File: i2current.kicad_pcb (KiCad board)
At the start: 2 copper layers, 59 parts, among them J1 Barrel_Jack_Switch, J2 USB_C_Receptacle_USB2.0, J3 CONN_BATT, J4 Lichtenprog_conn, Q1 WST03P06, Q2 MMBT2222A, Q3 MMBT2222A, SW1 SW_SPDT, U1 TPS61022, U2 BQ25606RGER, U3 SPX3819M5-L-3-3, U5 FUSB302B01MPX, U6 XT30(2+2)PW-M.G.B, U7 ESP32-C3-WROOM-02, U8 BQ25792RQMR

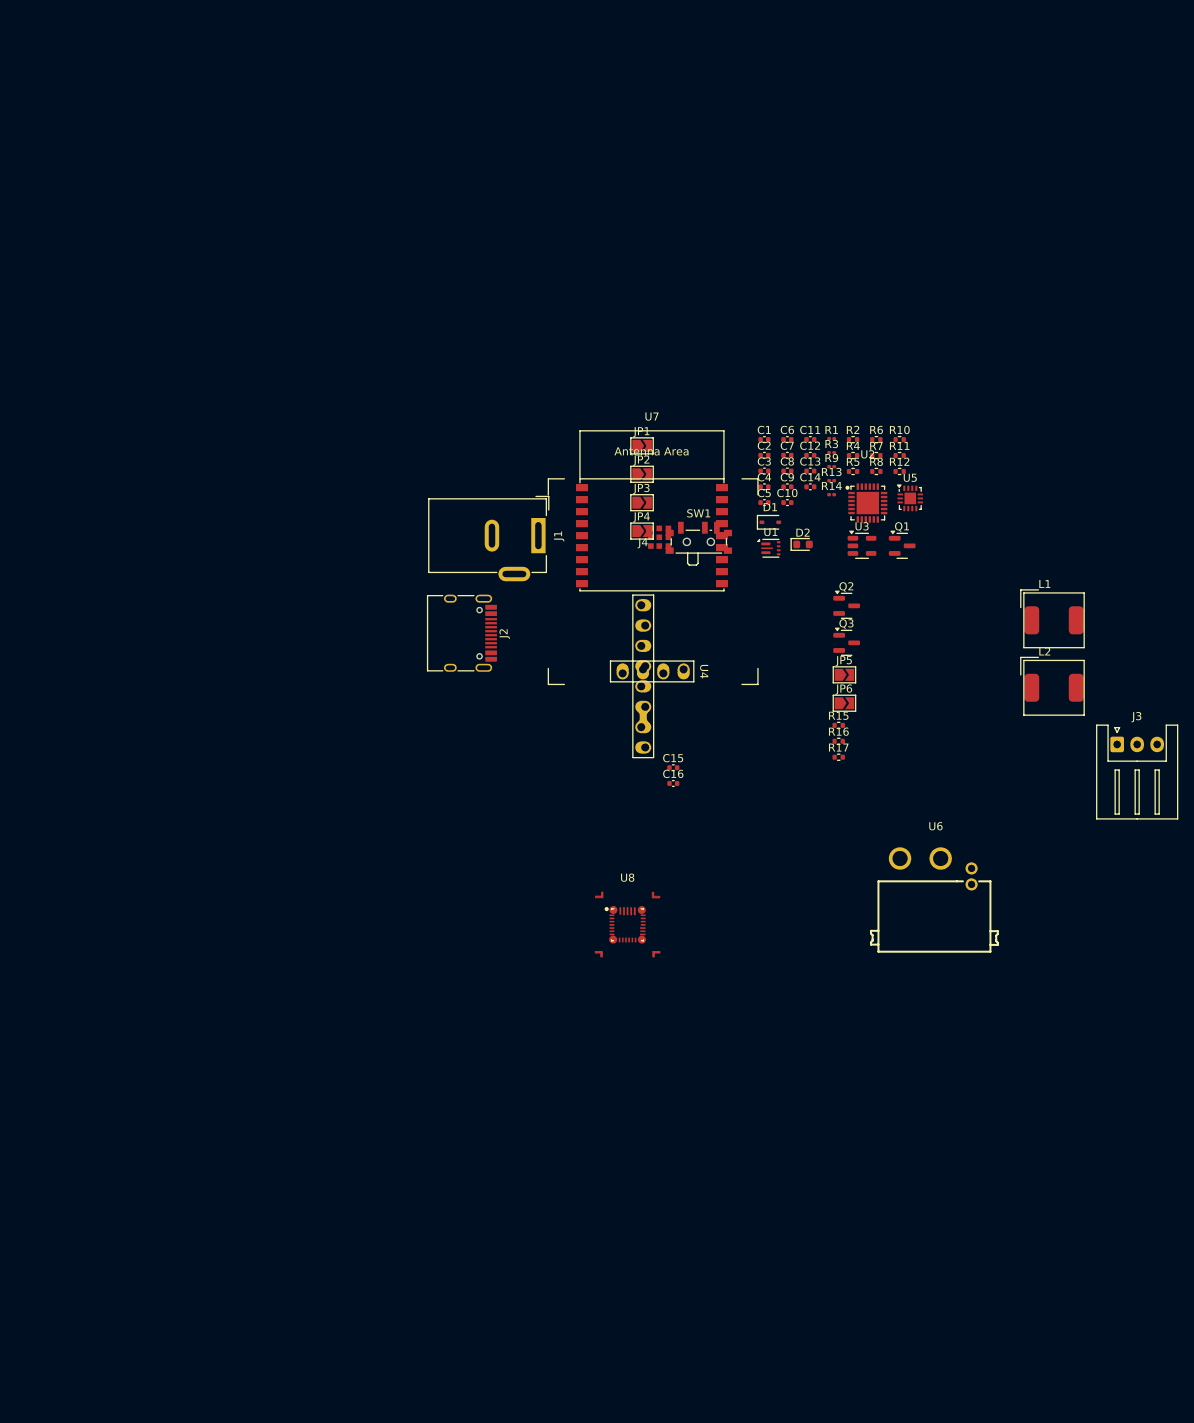
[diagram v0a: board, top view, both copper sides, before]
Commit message: connector placement
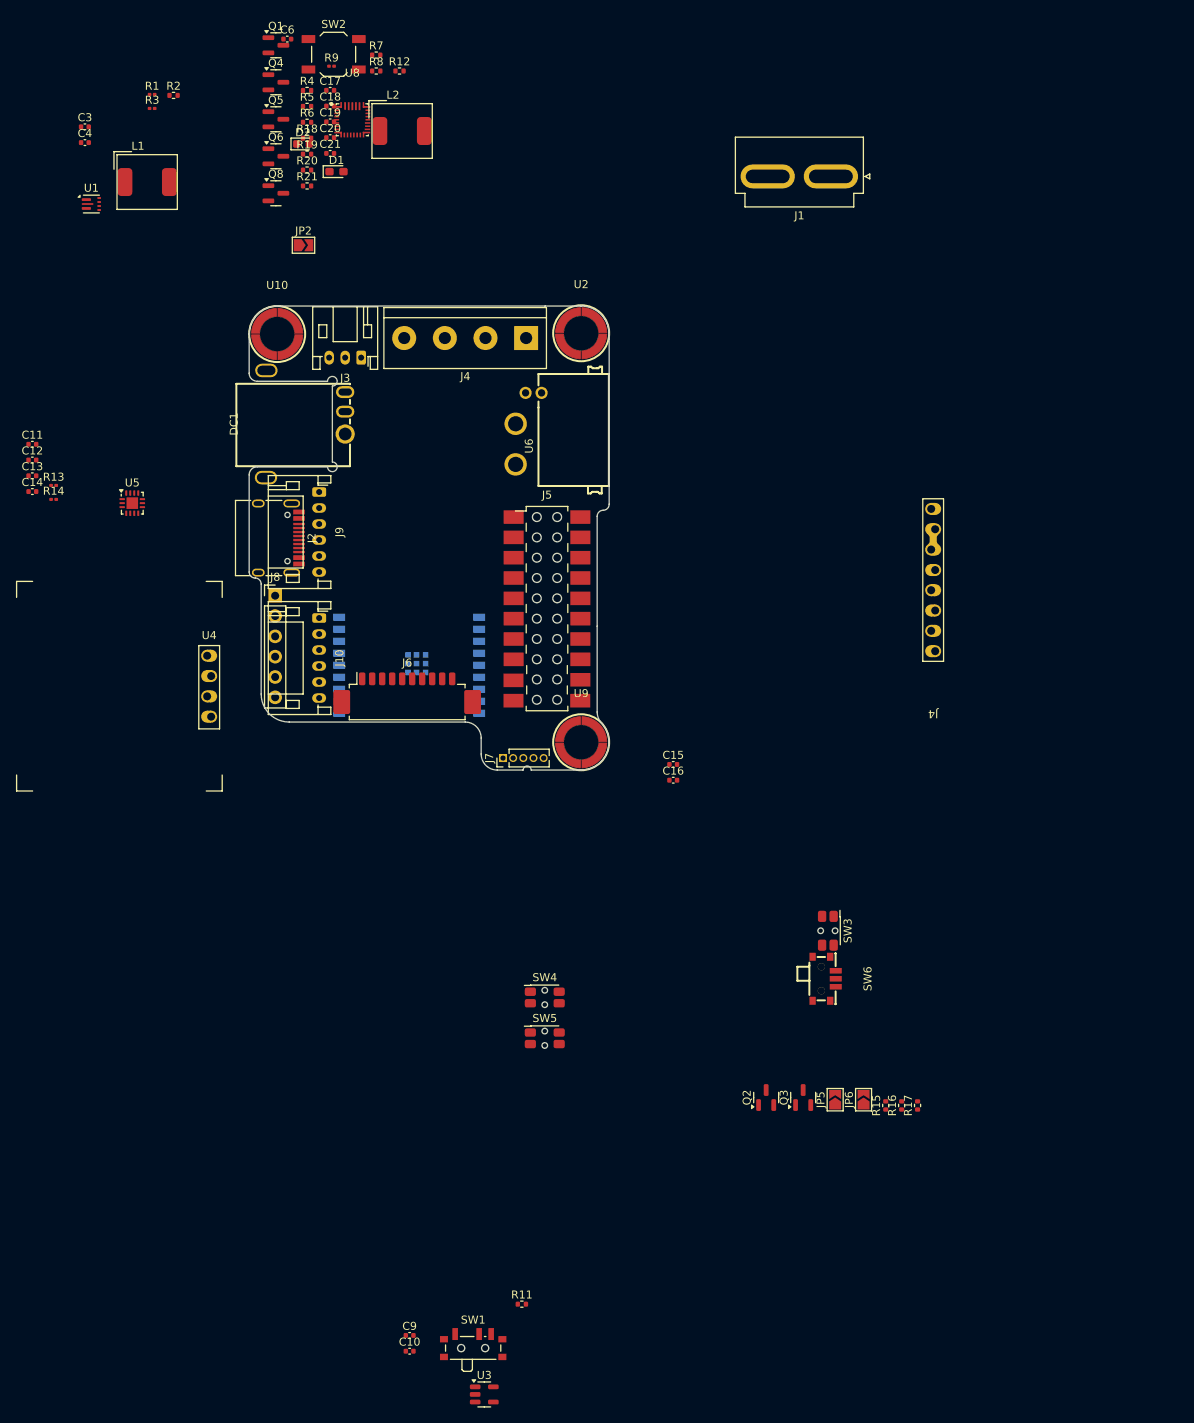
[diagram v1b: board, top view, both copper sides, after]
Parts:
- removed C1: 1u, Capacitor_SMD:C_0402_1005Metric
- removed C2, C8: 10u, Capacitor_SMD:C_0402_1005Metric
- removed C5: 100n, Capacitor_SMD:C_0402_1005Metric
- removed C7: 4.7u, Capacitor_SMD:C_0402_1005Metric
- removed JP1, JP3: SCH_BYP, Jumper:SolderJumper-2_P1.3mm_Open_TrianglePad1.0x1.5mm
- removed JP4: FUSB_INT, Jumper:SolderJumper-2_P1.3mm_Open_TrianglePad1.0x1.5mm
- removed R10: 240, Resistor_SMD:R_0402_1005Metric
- added C17: 10u, Capacitor_SMD:C_0402_1005Metric, F.Cu at (58.1, 27.5)
- added C18: 10u, Capacitor_SMD:C_0402_1005Metric, F.Cu at (58.1, 29.5)
- added C19: 100n, Capacitor_SMD:C_0402_1005Metric, F.Cu at (58.1, 31.5)
- added C20: 100n, Capacitor_SMD:C_0402_1005Metric, F.Cu at (58.1, 33.5)
- added C21: 10u, Capacitor_SMD:C_0402_1005Metric, F.Cu at (58.1, 35.4)
- added DC1: DC-C033D-5.5A-2.0, easyeda2kicad:DC-IN-TH_DC-C033D-5.5A-2.5, F.Cu at (55.1, 69.3)
- added J10: Conn_01x06, Connector_JST:JST_PH_S6B-PH-K_1x06_P2.00mm_Horizontal, F.Cu at (56.8, 93.5)
- added J4: Screw_Terminal_01x04, TerminalBlock:TerminalBlock_bornier-4_P5.08mm, F.Cu at (82.6, 58.5)
- added J5: EXT_IFACE, Critbit_lib:2x10_smdthrough, F.Cu at (85.2, 92.3)
- added J6: Conn_01x10, Connector_Molex:Molex_PicoBlade_53261-1071_1x10-1MP_P1.25mm_Horizontal, F.Cu at (67.8, 103.5)
- added J7: Conn_01x05, Connector_PinHeader_1.27mm:PinHeader_1x05_P1.27mm_Vertical, F.Cu at (79.7, 111.0)
- added J8: Conn_01x06, Connector_PinHeader_2.54mm:PinHeader_1x06_P2.54mm_Vertical, F.Cu at (51.2, 90.7)
- added J9: Conn_01x06, Connector_JST:JST_PH_S6B-PH-K_1x06_P2.00mm_Horizontal, F.Cu at (56.8, 77.8)
- added Q4: AO3400A, Package_TO_SOT_SMD:SOT-23, F.Cu at (51.3, 26.5)
- added Q5: AO3400A, Package_TO_SOT_SMD:SOT-23, F.Cu at (51.3, 31.2)
- added Q6: AO3400A, Package_TO_SOT_SMD:SOT-23, F.Cu at (51.3, 35.8)
- added Q8: AO3400A, Package_TO_SOT_SMD:SOT-23, F.Cu at (51.3, 40.4)
- added R18: 2k, Resistor_SMD:R_0402_1005Metric, F.Cu at (55.2, 33.5)
- added R19: 3k, Resistor_SMD:R_0402_1005Metric, F.Cu at (55.2, 35.5)
- added R20: 3k, Resistor_SMD:R_0402_1005Metric, F.Cu at (55.2, 37.5)
- added R21: 3k, Resistor_SMD:R_0402_1005Metric, F.Cu at (55.2, 39.5)
- added SW2: HARD_RST_BUT, Button_Switch_SMD:SW_SPST_TL3342, F.Cu at (58.6, 23.0)
- added SW3: B2, Button_Switch_SMD:SW_SPST_EVQP7C, F.Cu at (120.3, 132.6)
- added SW4: B2, Button_Switch_SMD:SW_SPST_EVQP7C, F.Cu at (85.0, 140.9)
- added SW5: B2, Button_Switch_SMD:SW_SPST_EVQP7C, F.Cu at (85.0, 146.0)
- added SW6: MINI MSK12CO2, easyeda2kicad:SW-SMD_MSK12CO2, F.Cu at (119.9, 138.6)
- added U10: SMTSO3030CTJ, easyeda2kicad:SMD_BD5.6-D4.1, F.Cu at (51.5, 58.0)
- added U9: SMTSO3030CTJ, easyeda2kicad:SMD_BD5.6-D4.1, F.Cu at (89.5, 109.0)
- D1: value 1N5819WS -> LED_0603; footprint Diode_SMD:D_SOD-323 -> LED_SMD:LED_0603_1608Metric_Pad1.05x0.95mm_HandSolder
- J1: value Barrel_Jack_Switch -> ~; footprint Connector_BarrelJack:BarrelJack_Wuerth_6941xx301002 -> Critbit_lib:B4P_MATRIXPWR
- J3: footprint Connector_JST:JST_XH_S3B-XH-A_1x03_P2.50mm_Horizontal -> Connector_JST:JST_PH_S3B-PH-K_1x03_P2.00mm_Horizontal
- Q1: value WST03P06 -> AO3400A
- R4: value 10k -> 450
- R5: value 0R -> 3k
- R6: value 450 -> 3k
- U2: value BQ25606RGER -> SMTSO3030CTJ; footprint easyeda2kicad:VQFN-24_L4.0-W4.0-P0.50-TL-EP2.8 -> easyeda2kicad:SMD_BD5.6-D4.1
- U7: moved to B.Cu
- moved L1 125.9 mm to (35.3, 39.0)
- moved C10 116.1 mm to (68.1, 185.1)
- moved C9 116.1 mm to (68.1, 183.2)
- moved R11 116.1 mm to (82.1, 179.3)
- moved U3 116.1 mm to (77.4, 190.6)
- moved L2 107.2 mm to (67.1, 32.6)
- moved U8 106.3 mm to (60.9, 31.2)
- moved J3 106.2 mm to (62.0, 61.0), turned to 180 degrees
- moved SW1 104.7 mm to (76.0, 184.4)
- moved Q1 100.2 mm to (51.3, 21.9)
- moved C11 97.3 mm to (20.9, 71.8)
- moved C12 97.3 mm to (20.9, 73.8)
- moved C13 97.3 mm to (20.9, 75.7)
- moved C14 97.3 mm to (20.9, 77.7)
- moved R13 97.3 mm to (23.6, 76.9)
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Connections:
- D1 pad 1: /BQ_PWR -> Net-(D1-K)
- J3 pad 1: BAT -> Net-(J3-Pin_1)
- L2 pad 1: Net-(C5-Pad2) -> Net-(U8-SW2)
- L2 pad 2: +BATT -> Net-(U8-SW1)
- Q1 pad 1: /PUSB_OFF -> Net-(Q1-G)
- Q1 pad 2: /BQ_PWR -> Net-(Q1-S)
- R12 pad 1: Net-(JP4-A) -> /SDA
- R4 pad 1: /PUSB_OFF -> Net-(U8-BATP)
- R4 pad 2: VBUS -> Net-(J3-Pin_1)
- R5 pad 1: Net-(U2-OTG) -> /SCL
- R5 pad 2: GND -> +3.3V
- R6 pad 1: Net-(U2-ICHG) -> /I2C_INT
- R6 pad 2: GND -> +3.3V
- R7 pad 2: Net-(U2-REGN) -> /BQ_REGN
- U2 pad 1: /BQ_PWR -> GND
- U2 pad 2: unconnected-(U2-NC-Pad2) -> (no net)
- U2 pad 3: unconnected-(U2-D+-Pad3) -> (no net)
- U2 pad 4: unconnected-(U2-D--Pad4) -> (no net)
- U4 pad 1: unconnected-(U4-GND-Pad1) -> GND
- U4 pad 2: unconnected-(U4-VCC-Pad2) -> +3.3V
- U4 pad 3: unconnected-(U4-SCL-Pad3) -> /SCL
- U4 pad 4: unconnected-(U4-SDA-Pad4) -> /SDA
- U5 pad 5: Net-(JP4-A) -> /I2C_INT
- U6 pad 2: unconnected-(U6-Pad2) -> GND
- U6 pad 3: unconnected-(U6-Pad3) -> /SDA
- U6 pad 4: unconnected-(U6-Pad4) -> /SCL
- U7 pad 8: /esp32-c3/IO9/BOOT_BUT1 -> /esp32-c3/IO9
- U8 pad 1: unconnected-(U8-STAT-Pad1) -> Net-(D1-K)
- U8 pad 10: unconnected-(U8-ACDRV2-Pad10) -> Net-(Q4-G)
- U8 pad 11: unconnected-(U8-ACDRV1-Pad11) -> Net-(Q1-G)
- U8 pad 12: unconnected-(U8-~{QON}-Pad12) -> /GLOB_RST
- U8 pad 13: unconnected-(U8-~{CE}-Pad13) -> +3.3V
- U8 pad 14: unconnected-(U8-SCL-Pad14) -> /SCL
- U8 pad 15: unconnected-(U8-SDA-Pad15) -> /SDA
- U8 pad 16: unconnected-(U8-TS-Pad16) -> Net-(J3-Pin_2)
- U8 pad 17: unconnected-(U8-ILIM_HIZ-Pad17) -> Net-(U8-ILIM_HIZ)
- U8 pad 18: unconnected-(U8-BATP-Pad18) -> Net-(U8-BATP)
- U8 pad 19: unconnected-(U8-BTST2-Pad19) -> Net-(U8-BTST2)
- U8 pad 20: unconnected-(U8-PROG-Pad20) -> Net-(U8-PROG)
- U8 pad 21: unconnected-(U8-~{INT}-Pad21) -> /I2C_INT
- U8 pad 24: unconnected-(U8-SDRV-Pad24) -> Net-(Q6-G)
- U8 pad 25: unconnected-(U8-SYS-Pad25) -> +BATT
- U8 pad 26: unconnected-(U8-SW2-Pad26) -> Net-(U8-SW2)
- U8 pad 27: unconnected-(U8-GND-Pad27) -> GND
- U8 pad 28: unconnected-(U8-SW1-Pad28) -> Net-(U8-SW1)
- U8 pad 29: unconnected-(U8-PMID-Pad29) -> Net-(U8-PMID)
- U8 pad 4: unconnected-(U8-BTST1-Pad4) -> Net-(U8-BTST1)
- U8 pad 5: unconnected-(U8-REGN-Pad5) -> /BQ_REGN
- U8 pad 8: unconnected-(U8-VAC2-Pad8) -> VBUS
- U8 pad 9: unconnected-(U8-VAC1-Pad9) -> +VDC
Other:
- board outline added: 45 x 58 mm
- board text added: "C500113"

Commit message: adadadadadadadadadada
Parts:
- removed J10: Conn_01x06, Connector_JST:JST_PH_S6B-PH-K_1x06_P2.00mm_Horizontal
- removed J4: Screw_Terminal_01x04, TerminalBlock:TerminalBlock_bornier-4_P5.08mm
- removed J4: Lichtenprog_conn, Critbit_lib:Lichtenprog
- removed JP5: 3V3_FROM_USBC, Jumper:SolderJumper-2_P1.3mm_Open_TrianglePad1.0x1.5mm
- removed JP6: PWR_FROM_USBC, Jumper:SolderJumper-2_P1.3mm_Open_TrianglePad1.0x1.5mm
- removed L2: L, Inductor_SMD:L_AVX_LMLP07A7
- removed Q2, Q3: MMBT2222A, Package_TO_SOT_SMD:SOT-23
- removed R11: 3k, Resistor_SMD:R_0402_1005Metric
- removed R14: 5.1k/DNP, Resistor_SMD:R_0201_0603Metric
- removed R16, R17: 10k, Resistor_SMD:R_0402_1005Metric
- removed SW1: SW_SPDT, Button_Switch_SMD:SW_SPDT_PCM12
- removed SW5: B2, Button_Switch_SMD:SW_SPST_EVQP7C
- removed U4: ~, Critbit_lib:OLED_4Pin_128x64_new
- added C1: 100n, Capacitor_SMD:C_0402_1005Metric, F.Cu at (67.5, 97.0)
- added C2: 100n, Capacitor_SMD:C_0402_1005Metric, F.Cu at (67.0, 98.5)
- added J11: Screw_Terminal_01x02, TerminalBlock_MetzConnect:TerminalBlock_MetzConnect_Type086_RT03402HBLC_1x02_P3.81mm_Horizontal, F.Cu at (68.4, 58.3)
- added J12: Screw_Terminal_01x02, TerminalBlock_MetzConnect:TerminalBlock_MetzConnect_Type086_RT03402HBLC_1x02_P3.81mm_Horizontal, F.Cu at (76.1, 58.3)
- added L3: FXL0420-1R0-M, easyeda2kicad:IND-SMD_L4.4-W4.2, F.Cu at (68.8, 66.4)
- added R10: 5.1k/DNP, Resistor_SMD:R_0603_1608Metric_Pad0.98x0.95mm_HandSolder, B.Cu at (51.2, 81.5)
- R13: footprint Resistor_SMD:R_0201_0603Metric -> Resistor_SMD:R_0603_1608Metric_Pad0.98x0.95mm_HandSolder; moved to B.Cu
- SW3, SW4: footprint Button_Switch_SMD:SW_SPST_EVQP7C -> Button_Switch_SMD:SW_SPST_TL3342
- SW6: value MINI MSK12CO2 -> SW_SPDT; footprint easyeda2kicad:SW-SMD_MSK12CO2 -> Button_Switch_THT:SW_Slide_SPDT_Angled_CK_OS102011MA1Q
- moved U3 93.4 mm to (64.4, 98.0)
- moved C10 87.9 mm to (61.5, 97.5), turned to -90 degrees
- moved C9 84.5 mm to (61.0, 99.0), turned to 180 degrees
- moved R15 84.4 mm to (56.8, 108.5)
- moved SW6 80.0 mm to (51.5, 97.2)
- moved R12 74.0 mm to (71.0, 99.0), turned to 180 degrees
- moved R5 71.7 mm to (73.2, 99.0)
- moved SW2 70.9 mm to (75.5, 91.8), turned to 90 degrees
- moved SW3 70.7 mm to (62.5, 91.8), turned to 90 degrees
- moved R6 68.9 mm to (69.0, 99.0)
- moved Q4 58.4 mm to (61.6, 84.0), turned to 180 degrees
- moved Q5 54.9 mm to (65.9, 84.0)
- moved Q1 52.6 mm to (63.5, 73.1), turned to 90 degrees
- moved SW4 51.6 mm to (69.0, 91.8), turned to 90 degrees
- moved C6 50.6 mm to (70.5, 68.5)
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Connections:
- net /GLOB_GPIO renamed /GLOB_GPIO2
- C13 pad 1: Net-(J2-CC1) -> /CC2
- C14 pad 1: Net-(J2-CC2) -> /CC1
- J2 pad A5: Net-(J2-CC1) -> /CC1
- J2 pad B5: Net-(J2-CC2) -> /CC2
- J5 pad 11: /I2C_INT -> /GLOB_RST
- J5 pad 13: /GLOB_RST -> /GLOB_GPIO1
- J5 pad 8: /V_OUT -> /I2C_INT
- J6 pad 1: unconnected-(J6-Pin_1-Pad1) -> +VDC
- J6 pad 10: unconnected-(J6-Pin_10-Pad10) -> /USBIN_P
- J6 pad 2: unconnected-(J6-Pin_2-Pad2) -> +BATT
- J6 pad 3: unconnected-(J6-Pin_3-Pad3) -> GND
- J6 pad 4: unconnected-(J6-Pin_4-Pad4) -> /I2C_INT
- J6 pad 5: unconnected-(J6-Pin_5-Pad5) -> +3.3V
- J6 pad 6: unconnected-(J6-Pin_6-Pad6) -> /SDA
- J6 pad 7: unconnected-(J6-Pin_7-Pad7) -> /SCL
- J6 pad 8: unconnected-(J6-Pin_8-Pad8) -> GND
- J6 pad 9: unconnected-(J6-Pin_9-Pad9) -> /USBIN_M
- J9 pad 1: unconnected-(J9-Pin_1-Pad1) -> GND
- J9 pad 2: unconnected-(J9-Pin_2-Pad2) -> /CC1
- J9 pad 3: unconnected-(J9-Pin_3-Pad3) -> /USBIN_M
- J9 pad 4: unconnected-(J9-Pin_4-Pad4) -> /USBIN_P
- J9 pad 5: unconnected-(J9-Pin_5-Pad5) -> /CC2
- J9 pad 6: unconnected-(J9-Pin_6-Pad6) -> VBUS
- Q1 pad 3: VBUS -> VBUS_PIN
- Q5 pad 3: VBUS -> VBUS_PIN
- R13 pad 2: Net-(J2-CC2) -> /CC2
- SW3 pad 1: unconnected-(SW3-Pad1) -> GND
- SW3 pad 2: unconnected-(SW3-Pad2) -> /esp32-c3/ESP_EN
- SW4 pad 1: unconnected-(SW4-Pad1) -> GND
- SW4 pad 2: unconnected-(SW4-Pad2) -> /esp32-c3/IO9
- U3 pad 3: Net-(SW1-B) -> +BATT
- U5 pad 1: Net-(J2-CC2) -> /CC2
- U5 pad 10: Net-(J2-CC1) -> /CC1
- U5 pad 11: Net-(J2-CC1) -> /CC1
- U5 pad 14: Net-(J2-CC2) -> /CC2
- U7 pad 6: /esp32-c3/IO7 -> /SCL
- U7 pad 7: /esp32-c3/IO8 -> /SDA
- U8 pad 2: VBUS -> VBUS_PIN
- U8 pad 3: VBUS -> VBUS_PIN
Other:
- board size 45 x 58 mm -> 45 x 76 mm
- board text added: "wystawac 1mm"
